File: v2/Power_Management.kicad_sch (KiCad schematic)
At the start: 14 parts, among them U7 INA219AIDCNR

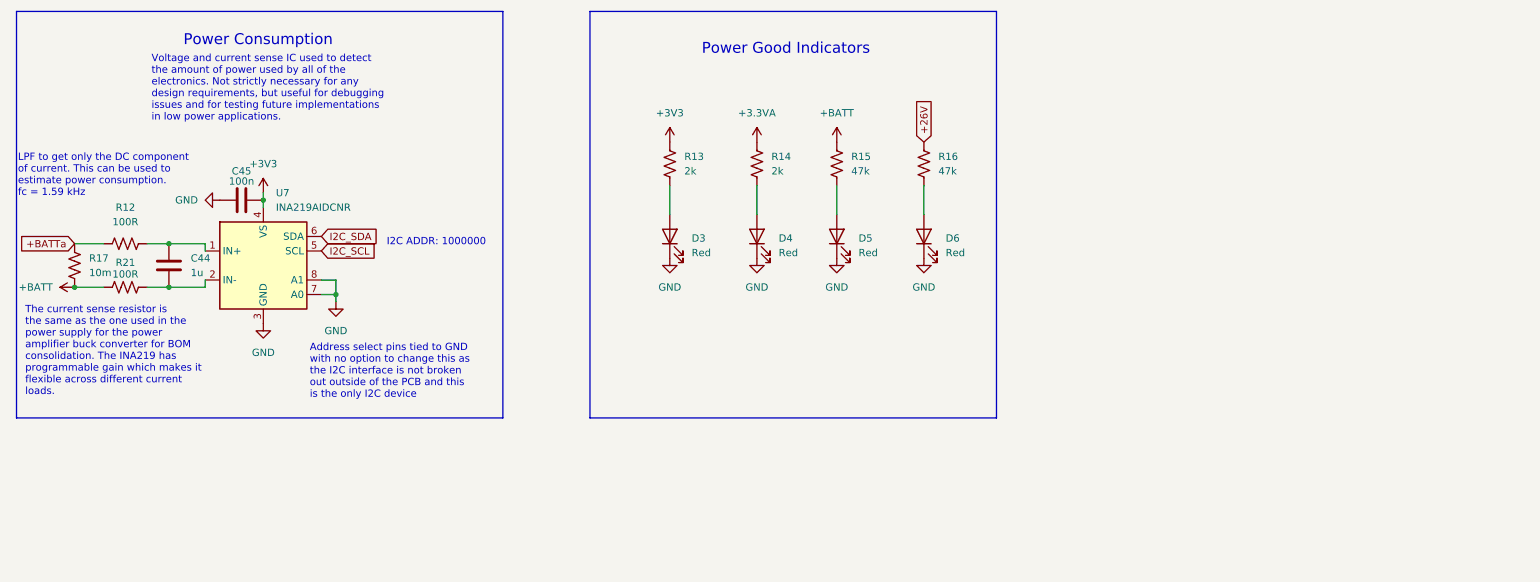
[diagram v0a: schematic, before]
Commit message: Most v2 changes made
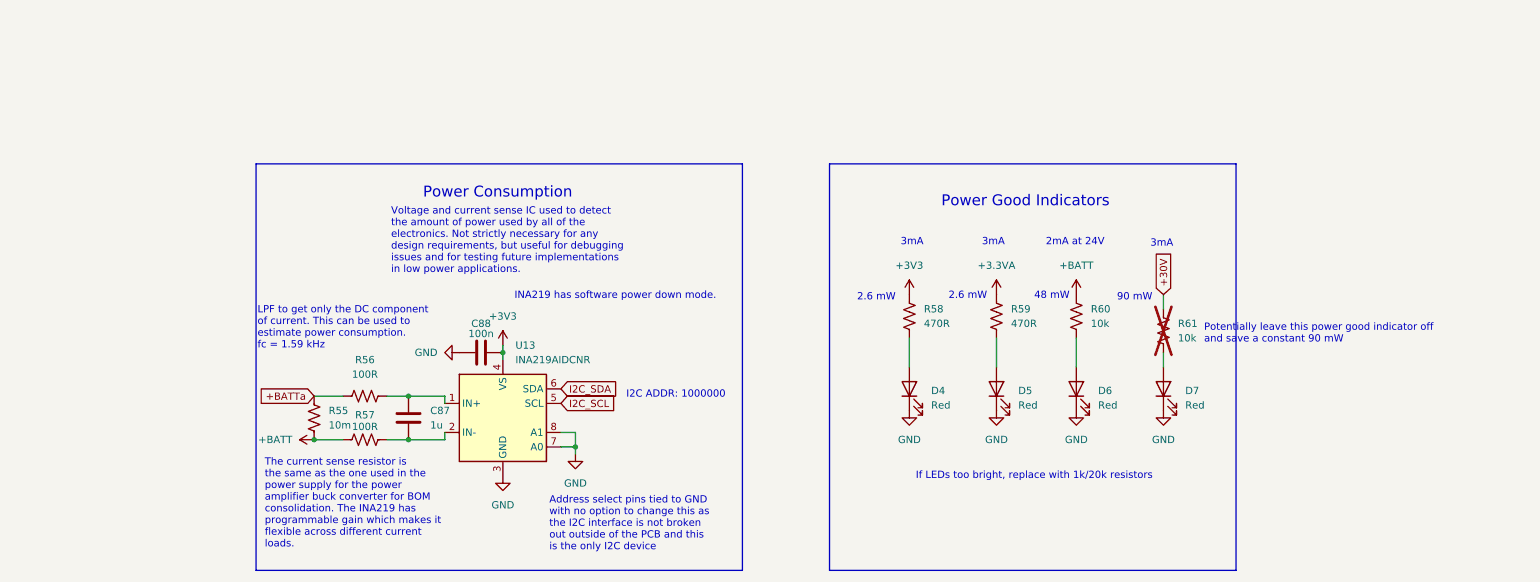
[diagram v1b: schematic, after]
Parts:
- removed C44: 1u, Capacitor_SMD:C_0603_1608Metric_Pad1.08x0.95mm_HandSolder, symbol UAM_symbols:C
- removed C45: 100n, Capacitor_SMD:C_0603_1608Metric_Pad1.08x0.95mm_HandSolder, symbol UAM_symbols:C
- removed R12, R21: 100R, Resistor_SMD:R_0603_1608Metric_Pad0.98x0.95mm_HandSolder, symbol UAM_symbols:R_US
- removed R13, R14: 2k, Resistor_SMD:R_0603_1608Metric_Pad0.98x0.95mm_HandSolder, symbol UAM_symbols:R_US
- removed R15, R16: 47k, Resistor_SMD:R_0603_1608Metric_Pad0.98x0.95mm_HandSolder, symbol UAM_symbols:R_US
- removed R17: 10m, Resistor_SMD:R_0805_2012Metric_Pad1.20x1.40mm_HandSolder, symbol UAM_symbols:R_US
- removed U7: INA219AIDCNR, Package_TO_SOT_SMD:SOT-23-8, symbol UAM_symbols:INA219AxDCN
- added C87: 1u, Capacitor_SMD:C_0603_1608Metric_Pad1.08x0.95mm_HandSolder, symbol UAM_symbols:C
- added C88: 100n, Capacitor_SMD:C_0603_1608Metric_Pad1.08x0.95mm_HandSolder, symbol UAM_symbols:C
- added R55: 10m, Resistor_SMD:R_0805_2012Metric_Pad1.20x1.40mm_HandSolder, symbol UAM_symbols:R_US
- added R56, R57: 100R, Resistor_SMD:R_0603_1608Metric_Pad0.98x0.95mm_HandSolder, symbol UAM_symbols:R_US
- added R58, R59: 470R, Resistor_SMD:R_0603_1608Metric_Pad0.98x0.95mm_HandSolder, symbol UAM_symbols:R_US
- added R60, R61: 10k, Resistor_SMD:R_0603_1608Metric_Pad0.98x0.95mm_HandSolder, symbol UAM_symbols:R_US
- added U13: INA219AIDCNR, Package_TO_SOT_SMD:SOT-23-8, symbol UAM_symbols:INA219AxDCN
- renumbered D3 to D4, D4 to D5, D5 to D6, D6 to D7
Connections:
- net +3.3VA: now also R59.2
- net +3V3: now also C88.2, R58.2, U13.4 (VS)
- net +BATT: now also R55.2, R57.1, R60.1
- net +BATTa: now also R55.1, R56.1
- net GND: now also C88.1, U13.3 (GND), U13.7 (A0), U13.8 (A1)
- net I2C_SCL: now also U13.5 (SCL)
- net I2C_SDA: now also U13.6 (SDA)
- net at D4.2 (A): now also R58.1
- net at D7.2 (A): now also R61.1
- net at D5.2 (A): now also R59.1
- net at D6.2 (A): now also R60.2
- new net: C87.1, R56.2, U13.1 (IN+)
- new net: C87.2, R57.2, U13.2 (IN-)
- new net +30V: R61.2
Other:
- note added: "2.6 mW"
- note added: "2mA at 24V"
- note added: "3mA"
- note added: "48 mW"
- note added: "90 mW"
- note added: "INA219 has software power down mode."
- note added: "If LEDs too bright, replace with 1k/20k resistors"
- note added: "Potentially leave this power good indicator off and save a constant 90 mW"
- company: Power Monitoring -> (none)
- title: EV -> (none)
- moved on the sheet: D4, D5, D6, D7
